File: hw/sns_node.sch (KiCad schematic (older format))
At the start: 15 parts

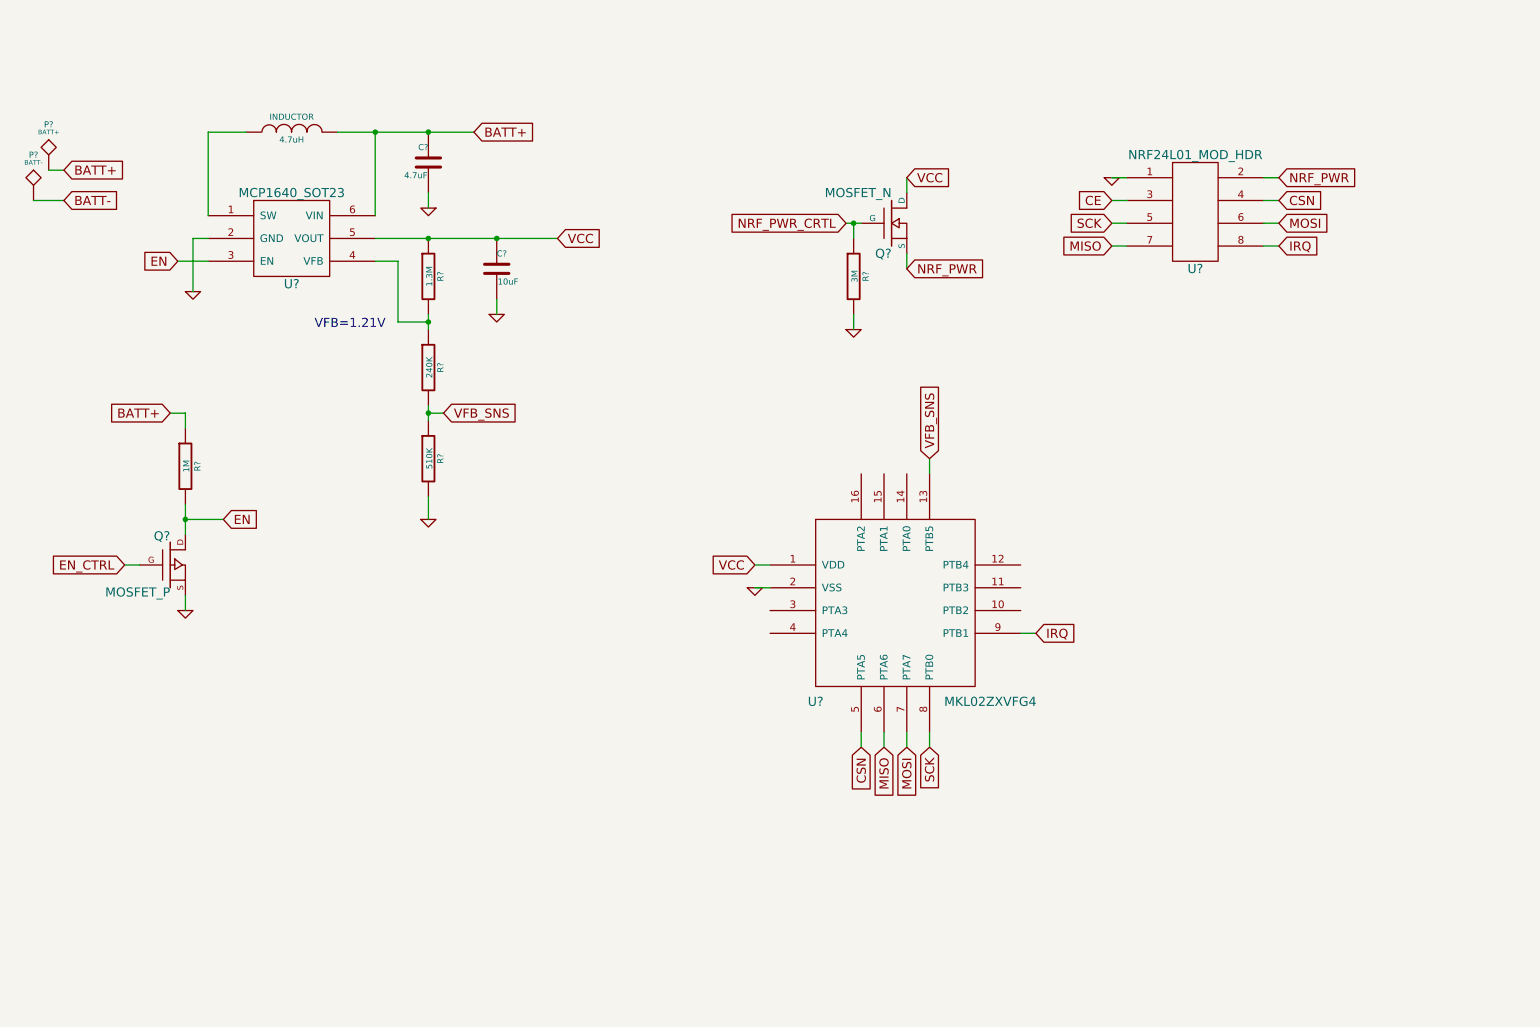
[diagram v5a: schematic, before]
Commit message: - schematic done, add net list
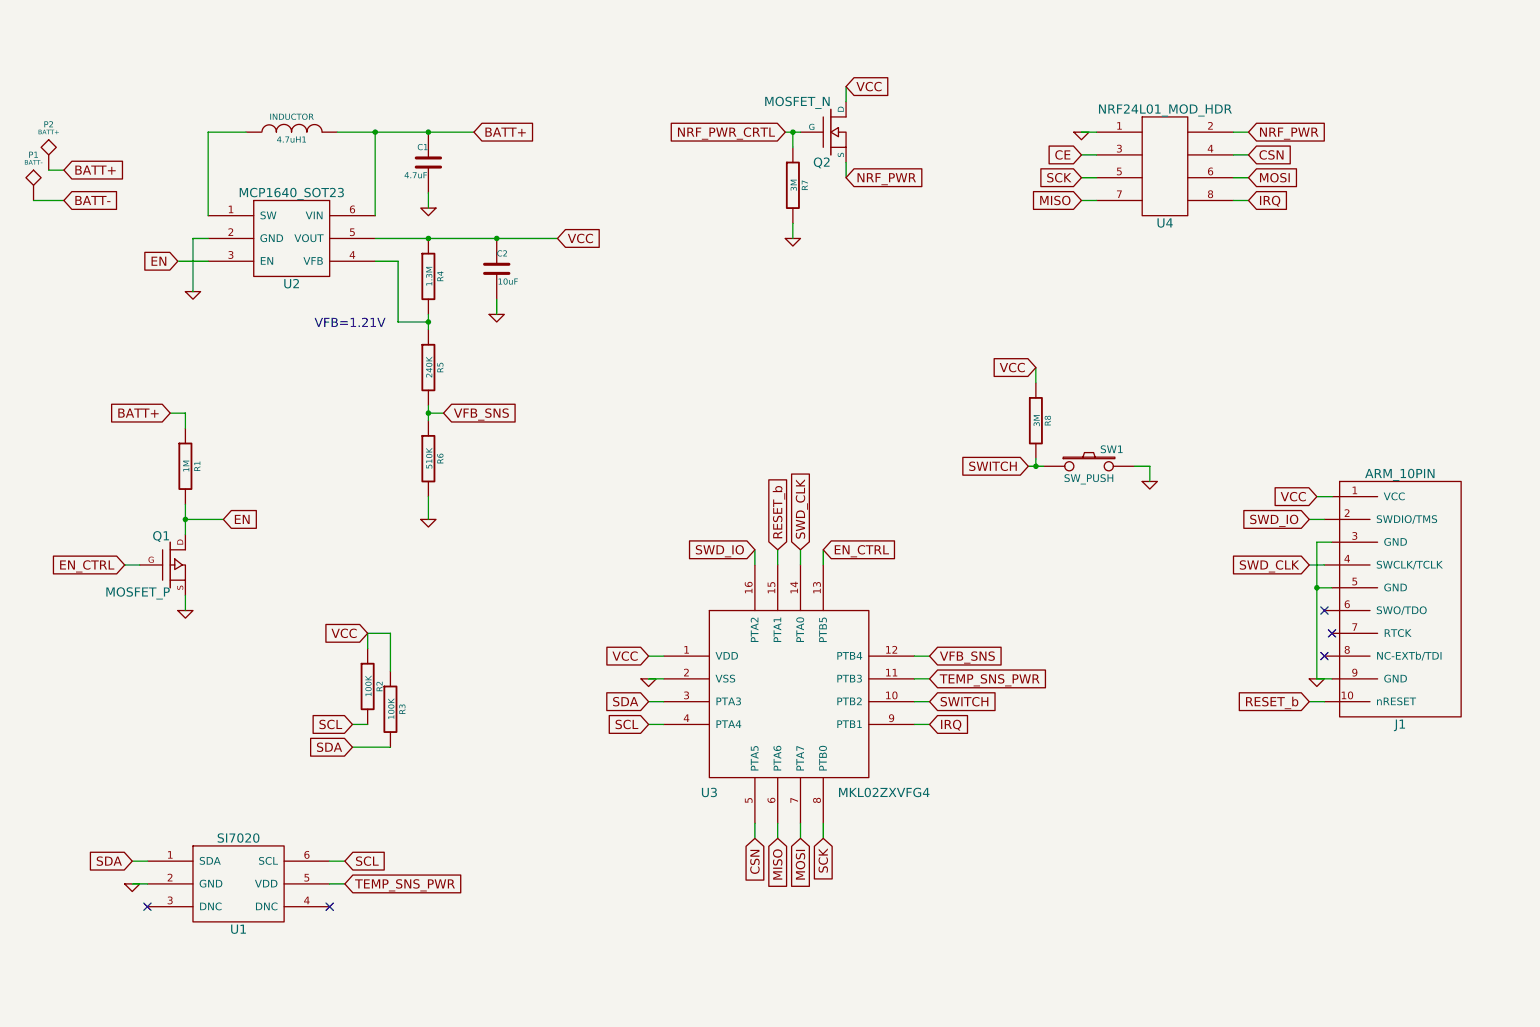
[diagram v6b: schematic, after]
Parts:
- added J1: ARM_10PIN, ~, symbol ARM_10PIN
- added R2, R3: 100K, ~, symbol R
- added R8: 3M, ~, symbol R
- added SW1: SW_PUSH, ~, symbol SW_PUSH
- added U1: SI7020, symbol SI7020
- gave numbers to parts that had none: 14
- renumbered 4.7uH to 4.7uH1
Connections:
- net EN_CTRL: now also U3.13 (PTB5)
- net GND: now also J1.3 (GND), J1.5 (GND), J1.9 (GND), SW1.2, U1.2 (GND)
- net VCC: now also J1.1 (VCC), R2.1, R3.1, R8.1
- net VFB_SNS: now also U3.12 (PTB4); no longer U3.13 (PTB5)
- net SWITCH: now reaches U3.10 (PTB2)
- net SWITCH: now also R8.2, SW1.1
- net TEMP_SNS_PWR: now reaches U3.11 (PTB3)
- net TEMP_SNS_PWR: now also U1.5 (VDD)
- net SWD_CLK: now reaches U3.14 (PTA0)
- net SWD_CLK: now also J1.4 (SWCLK/TCLK)
- net RESET_b: now reaches U3.15 (PTA1)
- net RESET_b: now also J1.10 (nRESET)
- net SWD_IO: now reaches U3.16 (PTA2)
- net SWD_IO: now also J1.2 (SWDIO/TMS)
- net SDA: now reaches U3.3 (PTA3)
- net SDA: now also R3.2, U1.1 (SDA)
- net SCL: now reaches U3.4 (PTA4)
- net SCL: now also R2.2, U1.6 (SCL)
- no-connect marks 0 -> 5
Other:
- moved on the sheet: Q2, R7, U3, U4

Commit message: - add usb voltage supply + ldo
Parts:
- added C3, C4: 1uF, ~, symbol C
- added J1: USB-MICRO-B, ~, symbol USB-MICRO-B
- added U6: AAT3220_SC-59-3, symbol AAT3220_SC-59-3
- renumbered J1 to J2, R4 to R2, R5 to R3, R6 to R4, R2 to R5, R3 to R6, 4.7uH1 to U2, U2 to U3, U3 to U4, U4 to U5
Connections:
- wire segments 76 -> 85
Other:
- moved on the sheet: J2, R5, R6, R8, SW1, U1, U4

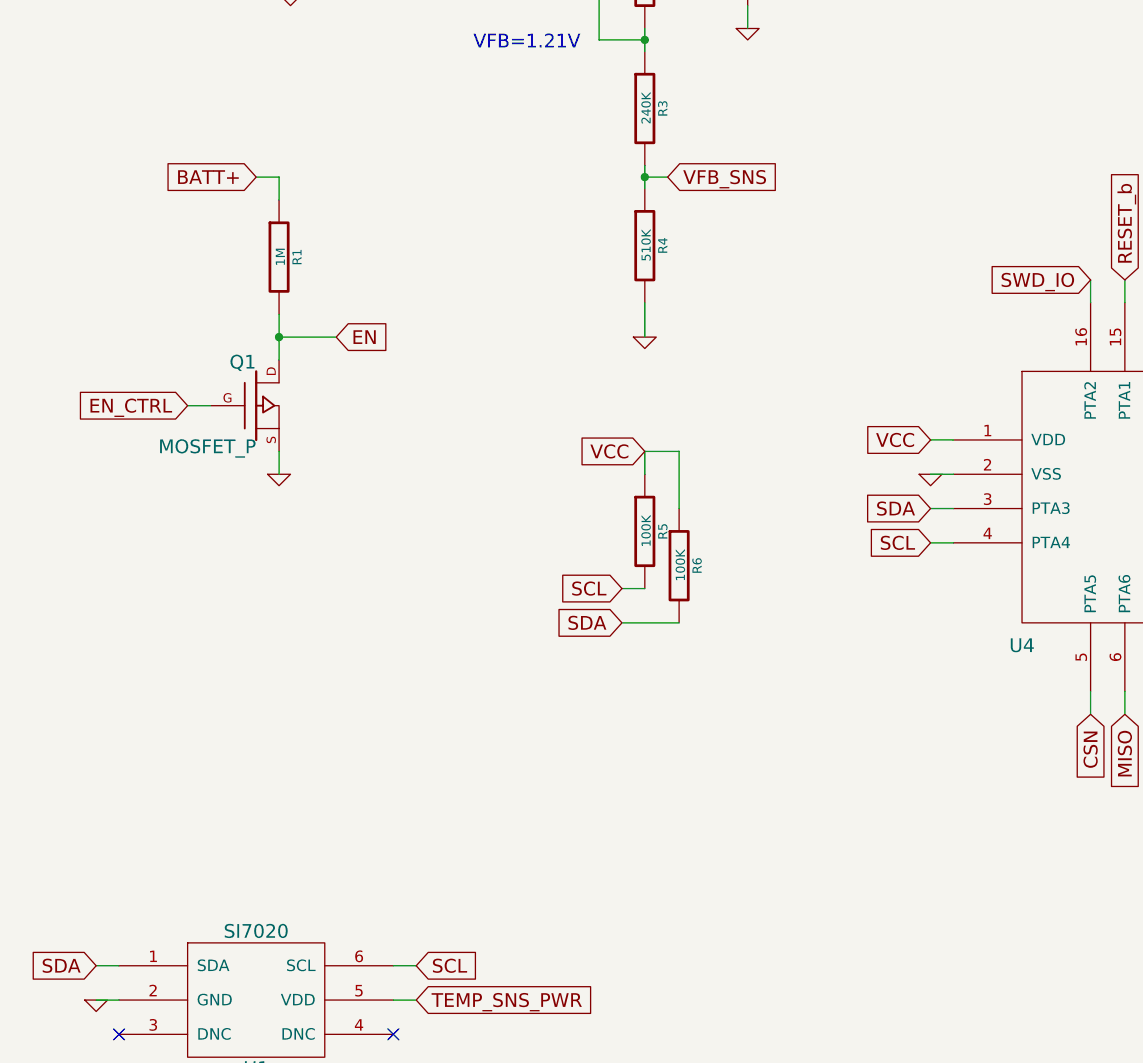
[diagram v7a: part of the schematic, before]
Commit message: - possible circuit to provide momentary turn on when battery is connected
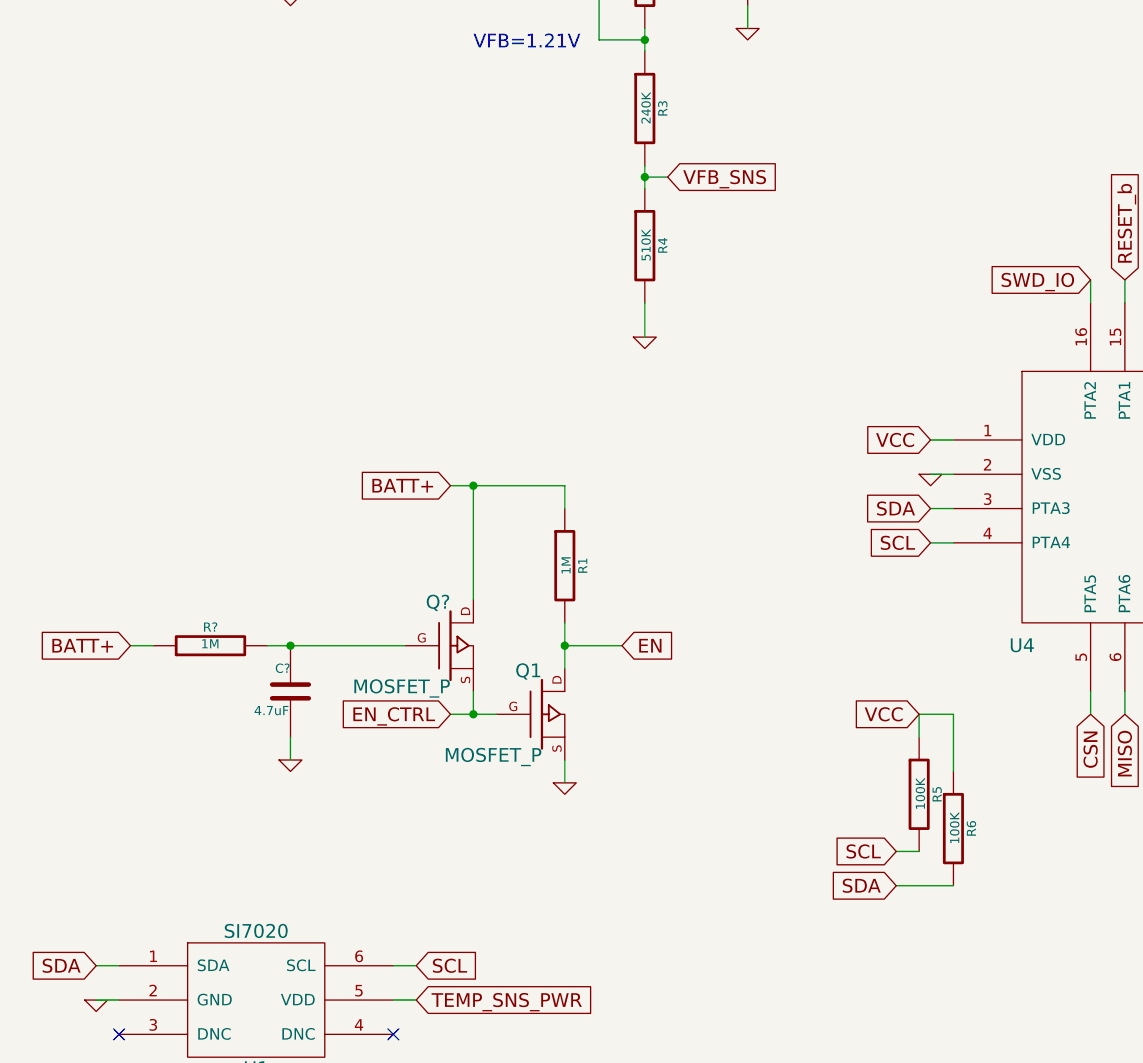
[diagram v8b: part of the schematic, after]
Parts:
- added C?: 4.7uF, ~, symbol C
- added Q?: MOSFET_P, ~, symbol MOSFET_P
- added R?: 1M, ~, symbol R
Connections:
- wire segments 85 -> 90
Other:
- moved on the sheet: Q1, R1, R5, R6
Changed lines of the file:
@@
 Sheet 1 1
 Title ""
-Date "20 feb 2014"
+Date "23 feb 2014"
 Rev ""
 Comp ""
@@
 Wire Wire Line
 	4650 4600 4750 4600
-Text GLabel 2050 4150 2    60   Input ~ 0
+Text GLabel 3300 5500 2    60   Input ~ 0
 EN
 $Comp
 L MOSFET_P Q1
 U 1 1 5302C7F0
-P 1700 4450
-F 0 "Q1" H 1700 4640 60  0000 R CNN
-F 1 "MOSFET_P" H 1700 4270 60  0000 R CNN
-F 2 "~" H 1700 4450 60  0000 C CNN
-F 3 "~" H 1700 4450 60  0000 C CNN
-	1    1700 4450
+P 2950 5800
+F 0 "Q1" H 2950 5990 60  0000 R CNN
+F 1 "MOSFET_P" H 2950 5620 60  0000 R CNN
+F 2 "~" H 2950 5800 60  0000 C CNN
+F 3 "~" H 2950 5800 60  0000 C CNN
+	1    2950 5800
 	1    0    0    -1
 $EndComp
@@
 L R R1
 U 1 1 5302C818
-P 1800 3800
-F 0 "R1" V 1880 3800 40  0000 C CNN
-F 1 "1M" V 1807 3801 40  0000 C CNN
-F 2 "~" V 1730 3800 30  0000 C CNN
-F 3 "~" H 1800 3800 30  0000 C CNN
-	1    1800 3800
-	1    0    0    -1
-$EndComp
-Wire Wire Line
-	2050 4150 1800 4150
-Wire Wire Line
-	1800 4050 1800 4250
-Connection ~ 1800 4150
-Text GLabel 1400 4450 0    60   Input ~ 0
+P 3050 5150
+F 0 "R1" V 3130 5150 40  0000 C CNN
+F 1 "1M" V 3057 5151 40  0000 C CNN
+F 2 "~" V 2980 5150 30  0000 C CNN
+F 3 "~" H 3050 5150 30  0000 C CNN
+	1    3050 5150
+	1    0    0    -1
+$EndComp
+Wire Wire Line
+	3300 5500 3050 5500
+Wire Wire Line
+	3050 5400 3050 5600
+Connection ~ 3050 5500
+Text GLabel 2550 5800 0    60   Input ~ 0
 EN_CTRL
 Wire Wire Line
-	1500 4450 1400 4450
-Text GLabel 1700 3450 0    60   Input ~ 0
+	2550 5800 2750 5800
+Text GLabel 2550 4800 0    60   Input ~ 0
 BATT+
 Wire Wire Line
-	1700 3450 1800 3450
-Wire Wire Line
-	1800 3450 1800 3550
+	2550 4800 3050 4800
+Wire Wire Line
+	3050 4800 3050 4900
 $Comp
 L GND #PWR06
 U 1 1 5302C99C
-P 1800 4750
-F 0 "#PWR06" H 1800 4750 30  0001 C CNN
-F 1 "GND" H 1800 4680 30  0001 C CNN
-F 2 "" H 1800 4750 60  0000 C CNN
-F 3 "" H 1800 4750 60  0000 C CNN
-	1    1800 4750
-	1    0    0    -1
-$EndComp
-Wire Wire Line
-	1800 4750 1800 4650
+P 3050 6100
+F 0 "#PWR06" H 3050 6100 30  0001 C CNN
+F 1 "GND" H 3050 6030 30  0001 C CNN
+F 2 "" H 3050 6100 60  0000 C CNN
+F 3 "" H 3050 6100 60  0000 C CNN
+	1    3050 6100
+	1    0    0    -1
+$EndComp
+Wire Wire Line
+	3050 6100 3050 6000
 $Comp
 L 2X4_HDR U5
@@
 NoConn ~ 9600 6100
 NoConn ~ 9550 6250
-Text GLabel 3300 5250 0    60   Input ~ 0
+Text GLabel 4500 6400 0    60   Input ~ 0
 SCL
-Text GLabel 3300 5400 0    60   Input ~ 0
+Text GLabel 4500 6550 0    60   Input ~ 0
 SDA
 $Comp
 L R R5
 U 1 1 53057A20
-P 3400 5000
-F 0 "R5" V 3480 5000 40  0000 C CNN
-F 1 "100K" V 3407 5001 40  0000 C CNN
-F 2 "~" V 3330 5000 30  0000 C CNN
-F 3 "~" H 3400 5000 30  0000 C CNN
-	1    3400 5000
+P 4600 6150
+F 0 "R5" V 4680 6150 40  0000 C CNN
+F 1 "100K" V 4607 6151 40  0000 C CNN
+F 2 "~" V 4530 6150 30  0000 C CNN
+F 3 "~" H 4600 6150 30  0000 C CNN
+	1    4600 6150
 	1    0    0    -1
 $EndComp
@@
 L R R6
 U 1 1 53057A31
-P 3550 5150
-F 0 "R6" V 3630 5150 40  0000 C CNN
-F 1 "100K" V 3557 5151 40  0000 C CNN
-F 2 "~" V 3480 5150 30  0000 C CNN
-F 3 "~" H 3550 5150 30  0000 C CNN
-	1    3550 5150
-	1    0    0    -1
-$EndComp
-Wire Wire Line
-	3400 5250 3300 5250
-Wire Wire Line
-	3300 5400 3550 5400
-Text GLabel 3400 4650 0    60   Input ~ 0
+P 4750 6300
+F 0 "R6" V 4830 6300 40  0000 C CNN
+F 1 "100K" V 4757 6301 40  0000 C CNN
+F 2 "~" V 4680 6300 30  0000 C CNN
+F 3 "~" H 4750 6300 30  0000 C CNN
+	1    4750 6300
+	1    0    0    -1
+$EndComp
+Wire Wire Line
+	4600 6400 4500 6400
+Wire Wire Line
+	4500 6550 4750 6550
+Text GLabel 4600 5800 0    60   Input ~ 0
 VCC
 Wire Wire Line
-	3400 4650 3400 4750
-Wire Wire Line
-	3400 4650 3550 4650
-Wire Wire Line
-	3550 4650 3550 4900
+	4600 5800 4600 5900
+Wire Wire Line
+	4600 5800 4750 5800
+Wire Wire Line
+	4750 5800 4750 6050
 $Comp
 L USB-MICRO-B J1
@@
 	9650 3850 9750 3850
 Connection ~ 9650 4000
+$Comp
+L MOSFET_P Q?
+U 1 1 53095B29
+P 2550 5500
+F 0 "Q?" H 2550 5690 60  0000 R CNN
+F 1 "MOSFET_P" H 2550 5320 60  0000 R CNN
+F 2 "~" H 2550 5500 60  0000 C CNN
+F 3 "~" H 2550 5500 60  0000 C CNN
+	1    2550 5500
+	1    0    0    -1
+$EndComp
+Wire Wire Line
+	2650 5800 2650 5700
+Connection ~ 2650 5800
+Wire Wire Line
+	2650 4800 2650 5300
+Connection ~ 2650 4800
+$Comp
+L R R?
+U 1 1 53095F19
+P 1500 5500
+F 0 "R?" V 1580 5500 40  0000 C CNN
+F 1 "1M" V 1507 5501 40  0000 C CNN
+F 2 "~" V 1430 5500 30  0000 C CNN
+F 3 "~" H 1500 5500 30  0000 C CNN
+	1    1500 5500
+	0    -1   -1   0
+$EndComp
+$Comp
+L C C?
+U 1 1 53095F1F
+P 1850 5700
+F 0 "C?" H 1850 5800 40  0000 L CNN
+F 1 "4.7uF" H 1856 5615 40  0000 L CNN
+F 2 "~" H 1888 5550 30  0000 C CNN
+F 3 "~" H 1850 5700 60  0000 C CNN
+	1    1850 5700
+	-1   0    0    -1
+$EndComp
+Wire Wire Line
+	1750 5500 2350 5500
+Connection ~ 1850 5500
+$Comp
+L GND #PWR?
+U 1 1 53096007
+P 1850 6000
+F 0 "#PWR?" H 1850 6000 30  0001 C CNN
+F 1 "GND" H 1850 5930 30  0001 C CNN
+F 2 "" H 1850 6000 60  0000 C CNN
+F 3 "" H 1850 6000 60  0000 C CNN
+	1    1850 6000
+	1    0    0    -1
+$EndComp
+Wire Wire Line
+	1850 6000 1850 5900
+Text GLabel 1150 5500 0    60   Input ~ 0
+BATT+
+Wire Wire Line
+	1150 5500 1250 5500
 $EndSCHEMATC
